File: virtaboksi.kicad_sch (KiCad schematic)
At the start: 29 parts, among them J1 Optional_01x03, J2 Ext_01x05, J3 Optional_01x02_Male, J4 Panel_01x08, J5 Powerpole 01x02, J6 Powerpole 01x02, J7 Powerpole 01x02, J8 TagConnect_TC2030-NL, U1 SRV05-4, U2 AMSRI-783.3-NZ, U3 SRV05-4, U4 SP3485EN, U5 STM8S003F3P

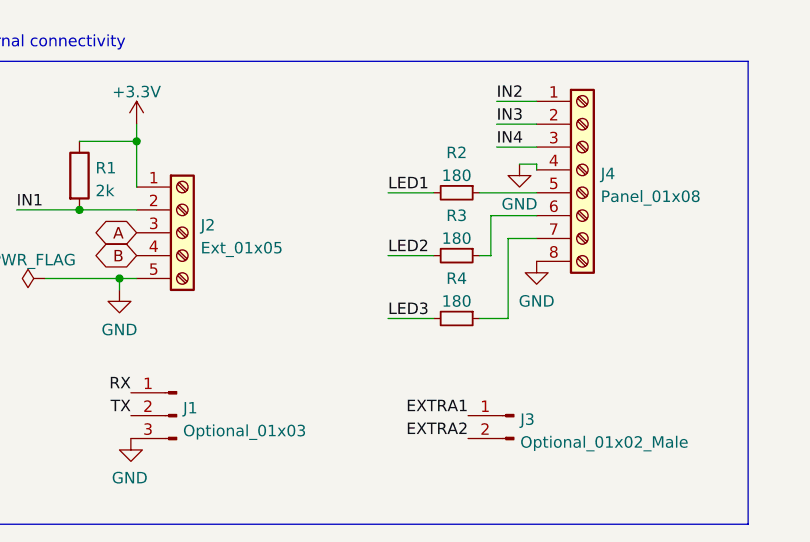
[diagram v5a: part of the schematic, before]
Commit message: Rename connectors J1-J4
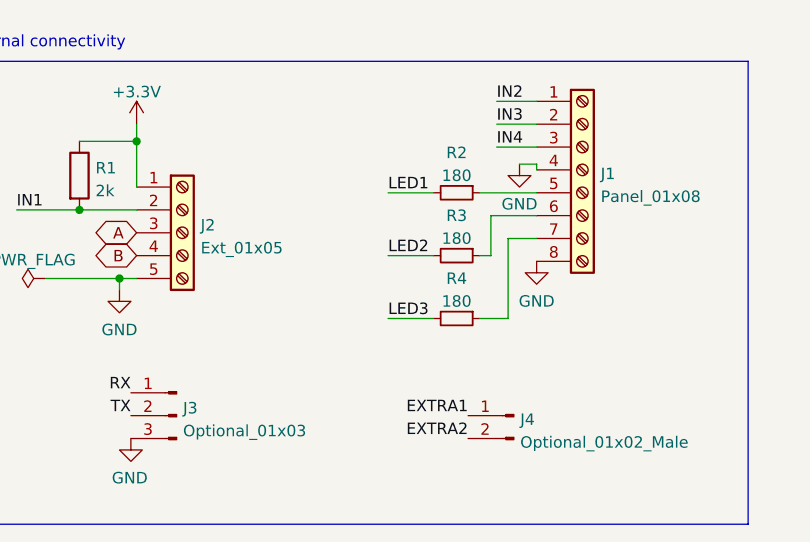
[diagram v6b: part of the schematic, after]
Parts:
- renumbered J4 to J1, J1 to J3, J3 to J4
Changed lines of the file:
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@@
   (symbol (lib_id "Connector:Screw_Terminal_01x08") (at 158.75 121.92 0) (unit 1)
     (in_bom yes) (on_board yes) (fields_autoplaced)
-    (property "Reference" "J4" (id 0) (at 160.782 122.3553 0)
+    (property "Reference" "J1" (id 0) (at 160.782 122.3553 0)
       (effects (font (size 1.27 1.27)) (justify left))
     )
@@
   (symbol (lib_id "Connector:Conn_01x03_Male") (at 113.665 149.225 0) (mirror y) (unit 1)
     (in_bom yes) (on_board yes) (fields_autoplaced)
-    (property "Reference" "J1" (id 0) (at 114.3762 148.3903 0)
+    (property "Reference" "J3" (id 0) (at 114.3762 148.3903 0)
       (effects (font (size 1.27 1.27)) (justify right))
     )
@@
   (symbol (lib_id "Connector:Conn_01x02_Male") (at 151.13 149.225 0) (mirror y) (unit 1)
     (in_bom yes) (on_board yes) (fields_autoplaced)
-    (property "Reference" "J3" (id 0) (at 151.8412 149.6603 0)
+    (property "Reference" "J4" (id 0) (at 151.8412 149.6603 0)
       (effects (font (size 1.27 1.27)) (justify right))
     )
@@
       (reference "HS6") (unit 1) (value "Heatsink") (footprint "Own parts:Heatsink_AAVID_576802B03900G-nocourt")
     )
-    (path "/39843b1b-17bb-49a5-b7e1-93a1228767c3"
-      (reference "J1") (unit 1) (value "Optional_01x03") (footprint "Connector_PinHeader_2.54mm:PinHeader_1x03_P2.54mm_Vertical")
+    (path "/1bb20b60-c240-45a3-8b39-4a64e7d30638"
+      (reference "J1") (unit 1) (value "Panel_01x08") (footprint "Connector_Phoenix_MC:PhoenixContact_MCV_1,5_8-G-3.5_1x08_P3.50mm_Vertical")
     )
     (path "/16cdac4d-aef8-4a03-ba0c-34d3de957317"
       (reference "J2") (unit 1) (value "Ext_01x05") (footprint "Connector_Phoenix_MC:PhoenixContact_MCV_1,5_5-G-3.5_1x05_P3.50mm_Vertical")
     )
+    (path "/39843b1b-17bb-49a5-b7e1-93a1228767c3"
+      (reference "J3") (unit 1) (value "Optional_01x03") (footprint "Connector_PinHeader_2.54mm:PinHeader_1x03_P2.54mm_Vertical")
+    )
     (path "/91bec629-c4a6-47bd-a435-b57ee40d6d6b"
-      (reference "J3") (unit 1) (value "Optional_01x02_Male") (footprint "Connector_PinHeader_2.54mm:PinHeader_1x02_P2.54mm_Vertical")
-    )
-    (path "/1bb20b60-c240-45a3-8b39-4a64e7d30638"
-      (reference "J4") (unit 1) (value "Panel_01x08") (footprint "Connector_Phoenix_MC:PhoenixContact_MCV_1,5_8-G-3.5_1x08_P3.50mm_Vertical")
+      (reference "J4") (unit 1) (value "Optional_01x02_Male") (footprint "Connector_PinHeader_2.54mm:PinHeader_1x02_P2.54mm_Vertical")
     )
     (path "/590d2007-4432-4cf1-bed4-e278a0f0bbe5"

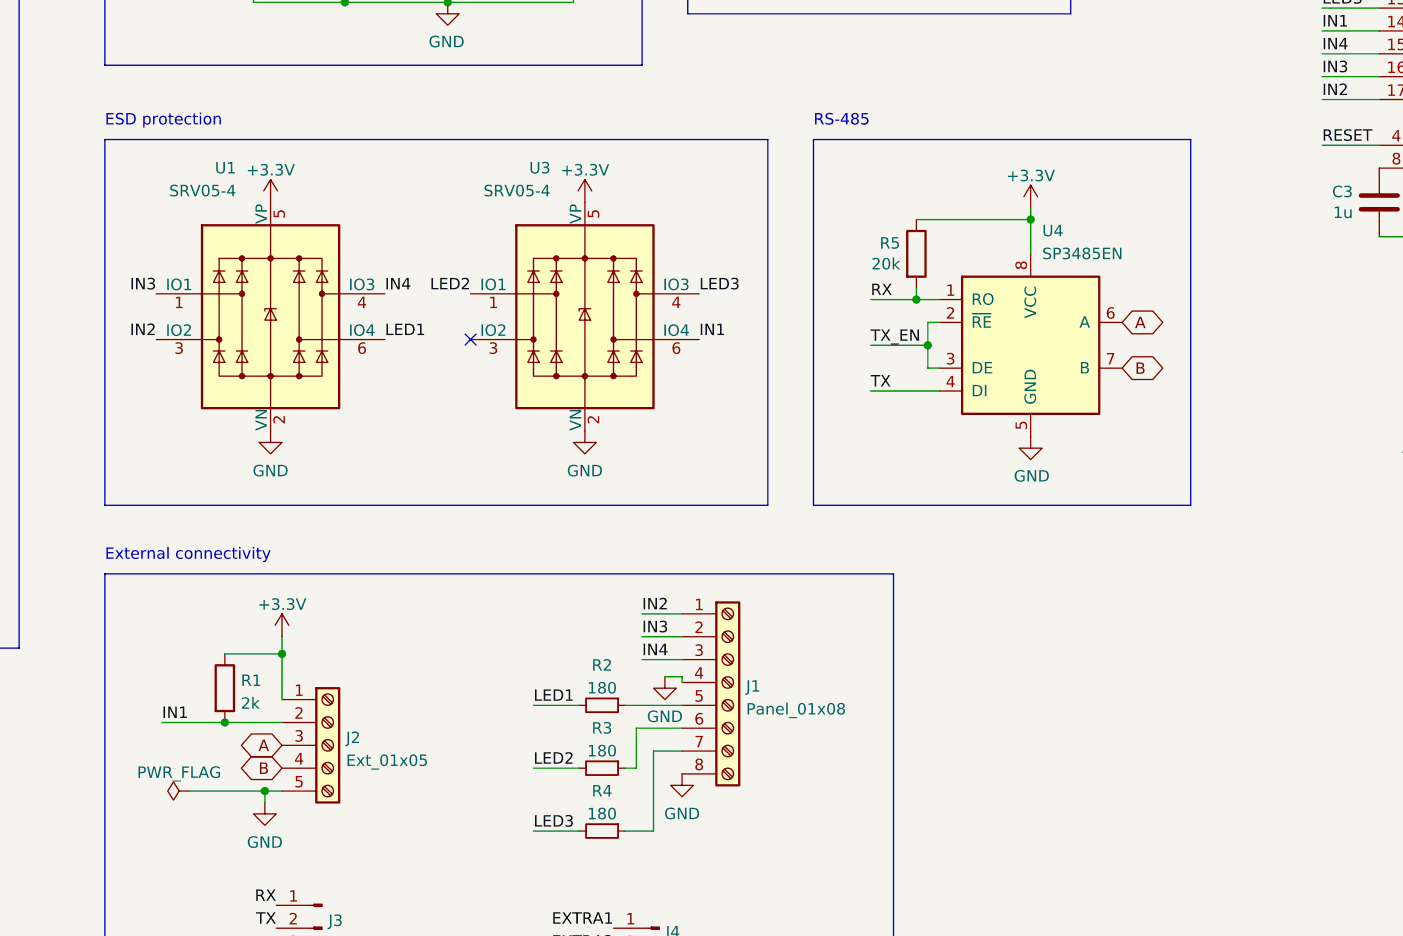
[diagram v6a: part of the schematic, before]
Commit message: Add stronger pull-ups for inputs
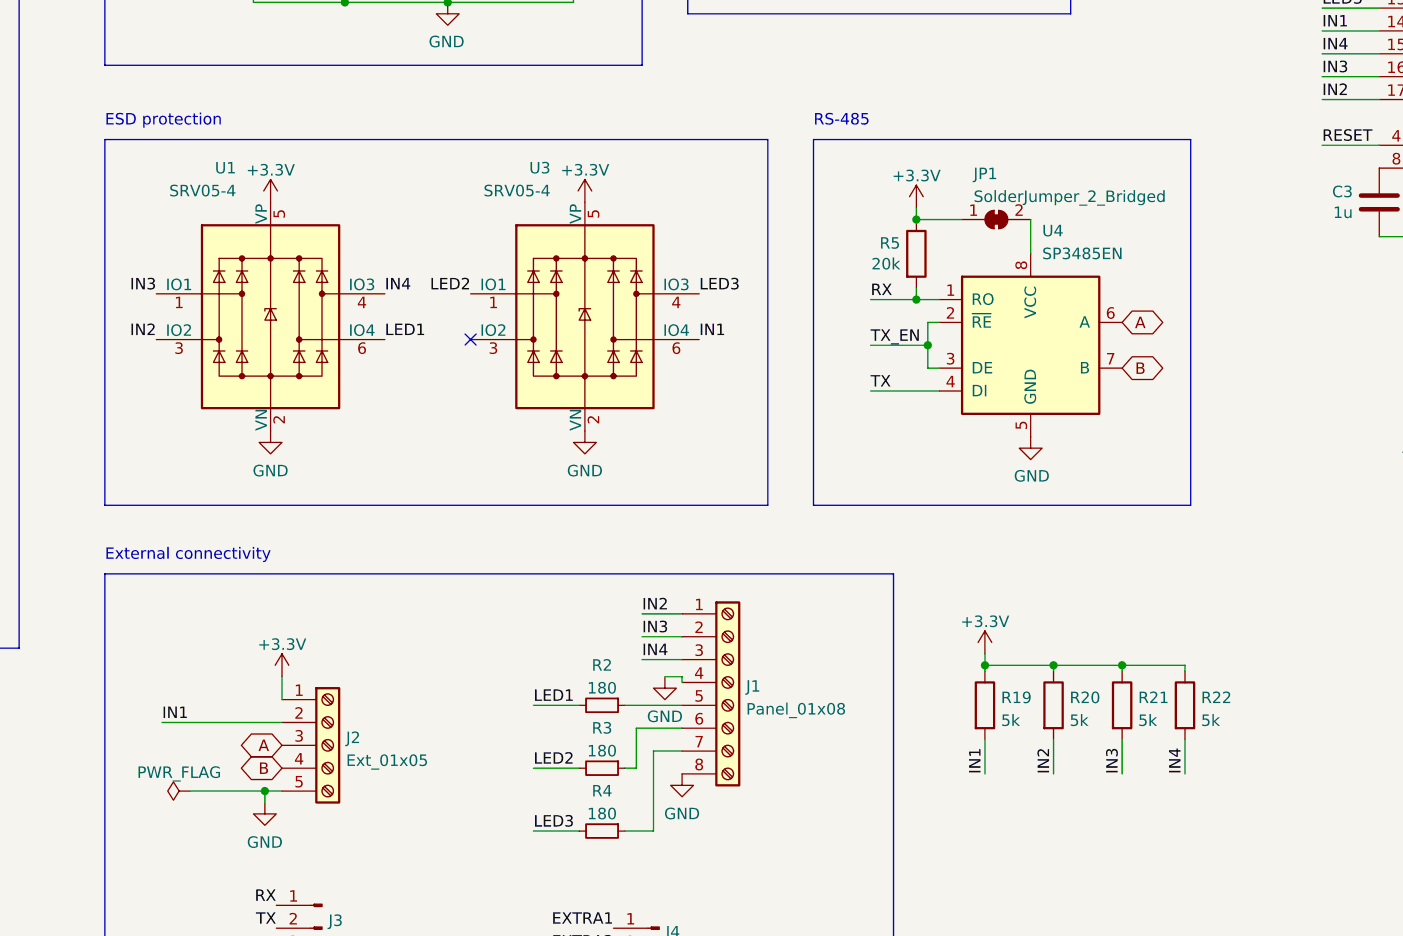
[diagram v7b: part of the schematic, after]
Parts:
- added JP1: SolderJumper_2_Bridged, Jumper:SolderJumper-2_P1.3mm_Bridged_Pad1.0x1.5mm, symbol Jumper:SolderJumper_2_Bridged
- added R20, R21, R22: 5k, Resistor_SMD:R_0603_1608Metric, symbol Device:R
- R19: renamed from R1; value 2k -> 5k; LCSC C22975 -> C22843
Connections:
- net +3.3V: now also JP1.1 (A), R20.1, R21.1, R22.1; no longer U4.8 (VCC)
- net IN2: now also R20.2
- net IN3: now also R21.2
- net IN4: now also R22.2
- new net: JP1.2 (B), U4.8 (VCC)
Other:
- moved on the sheet: R19

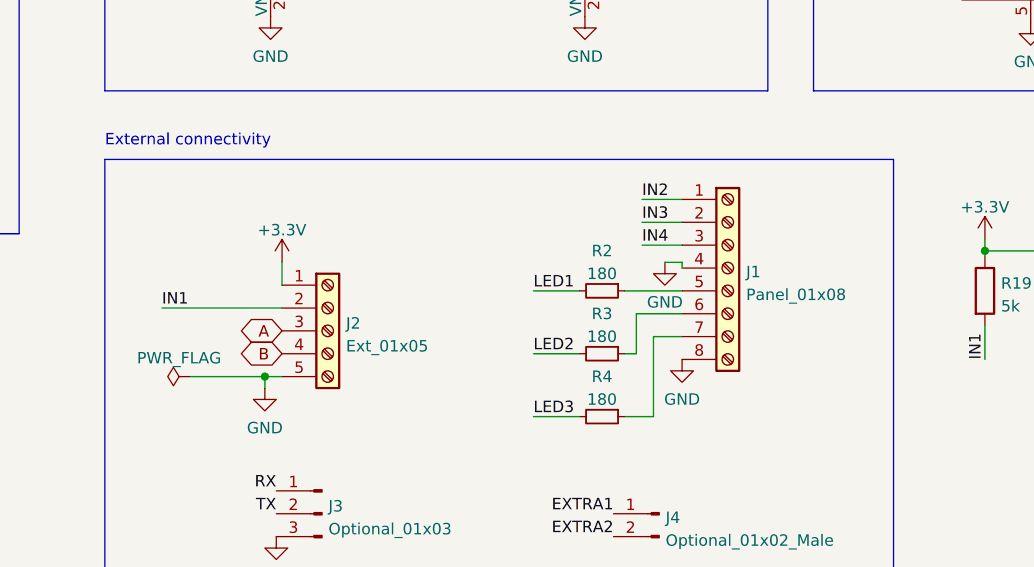
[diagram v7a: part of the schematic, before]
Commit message: Move one input to external connector, make them same length
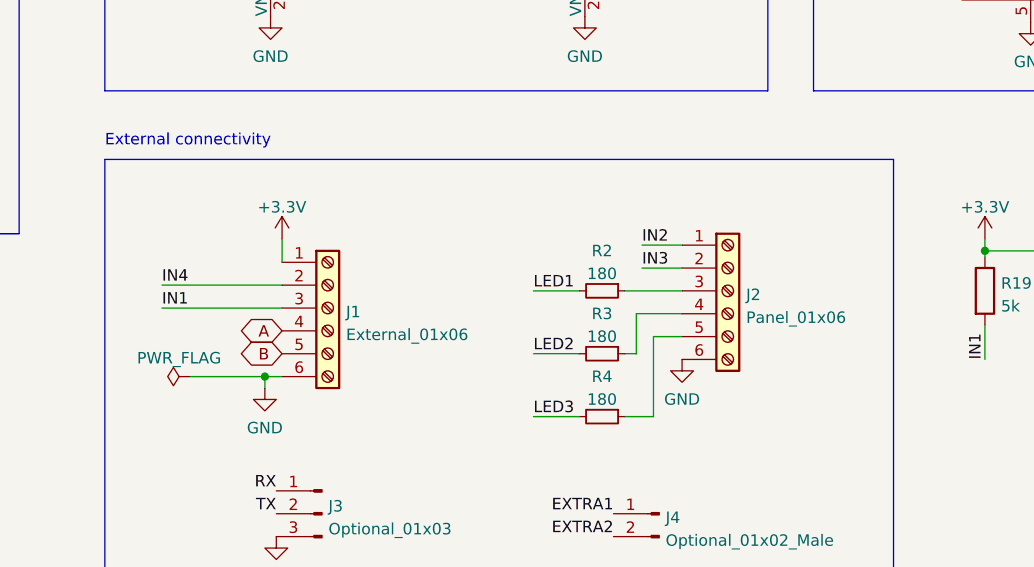
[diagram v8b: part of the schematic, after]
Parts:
- removed J1: Panel_01x08, Connector_Phoenix_MC:PhoenixContact_MCV_1,5_8-G-3.5_1x08_P3.50mm_Vertical, symbol Connector:Screw_Terminal_01x08
- removed J2: Ext_01x05, Connector_Phoenix_MC:PhoenixContact_MCV_1,5_5-G-3.5_1x05_P3.50mm_Vertical, symbol Connector:Screw_Terminal_01x05
- added J1: External_01x06, Connector_Phoenix_MC:PhoenixContact_MCV_1,5_6-G-3.5_1x06_P3.50mm_Vertical, symbol Connector:Screw_Terminal_01x06
- added J2: Panel_01x06, Connector_Phoenix_MC:PhoenixContact_MCV_1,5_6-G-3.5_1x06_P3.50mm_Vertical, symbol Connector:Screw_Terminal_01x06
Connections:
- net +3.3V: now also J1.1 (Pin_1)
- net A: now also J1.4 (Pin_4)
- net B: now also J1.5 (Pin_5)
- net GND: now also J1.6 (Pin_6), J2.6 (Pin_6)
- net IN1: now also J1.3 (Pin_3)
- net IN2: now also J2.1 (Pin_1)
- net IN3: now also J2.2 (Pin_2)
- net IN4: now also J1.2 (Pin_2)
- net at R4.1: now also J2.5 (Pin_5)
- net at R2.1: now also J2.3 (Pin_3)
- net at R3.1: now also J2.4 (Pin_4)
